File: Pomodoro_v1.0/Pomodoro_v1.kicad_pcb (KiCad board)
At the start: 2 copper layers, 70 x 50 mm, 91 parts, among them J1 BATT, J13 SWIM, J3 USB_OTG, J5 UART, M1 MOUNTING-HOLE, M2 MOUNTING-HOLE, M3 MOUNTING-HOLE, M4 MOUNTING-HOLE, Q1 BC807, Q2 BC807, SW1 SLIDER, SW2 BUTTON_SPST, U1 MCP73833, U2 TPS62260, U3 STM8L151C2T6, U4 AS1122

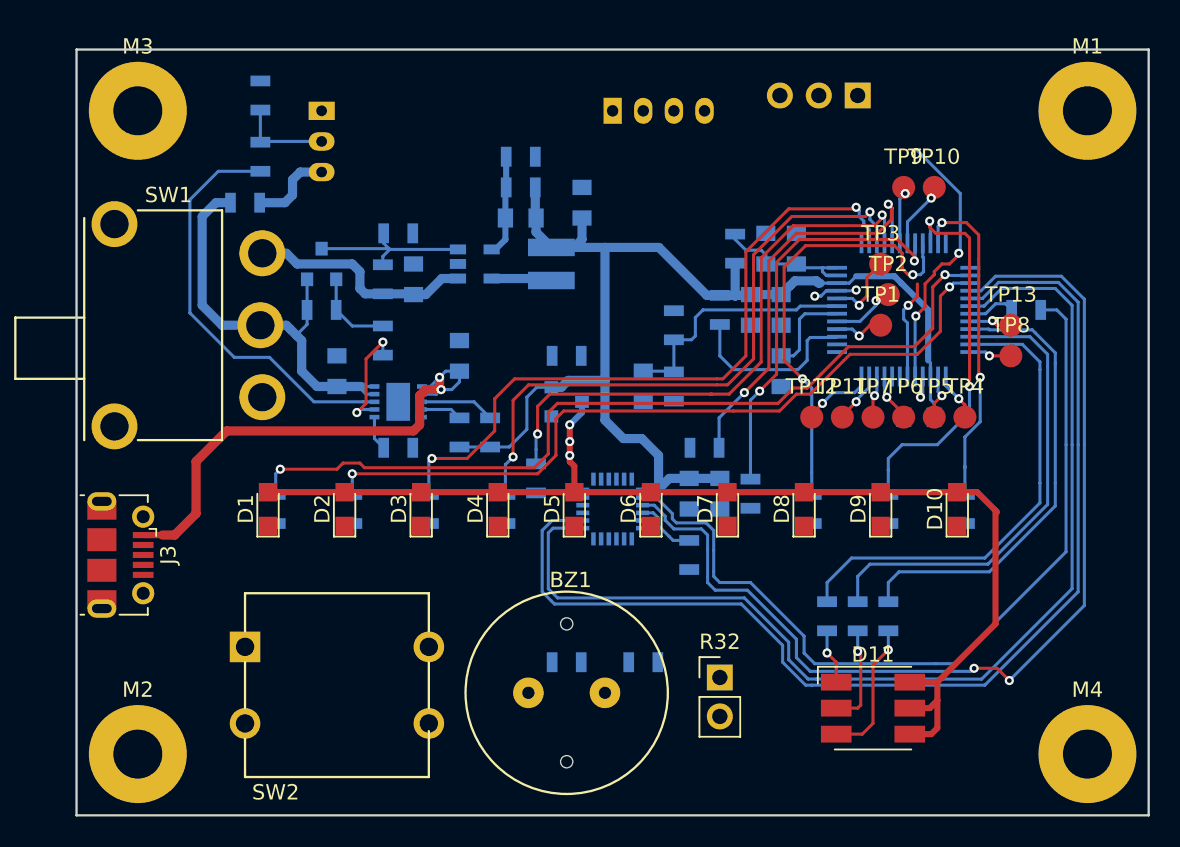
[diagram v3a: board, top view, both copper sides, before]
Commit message: all signals are routed, need to fix a few GND connections
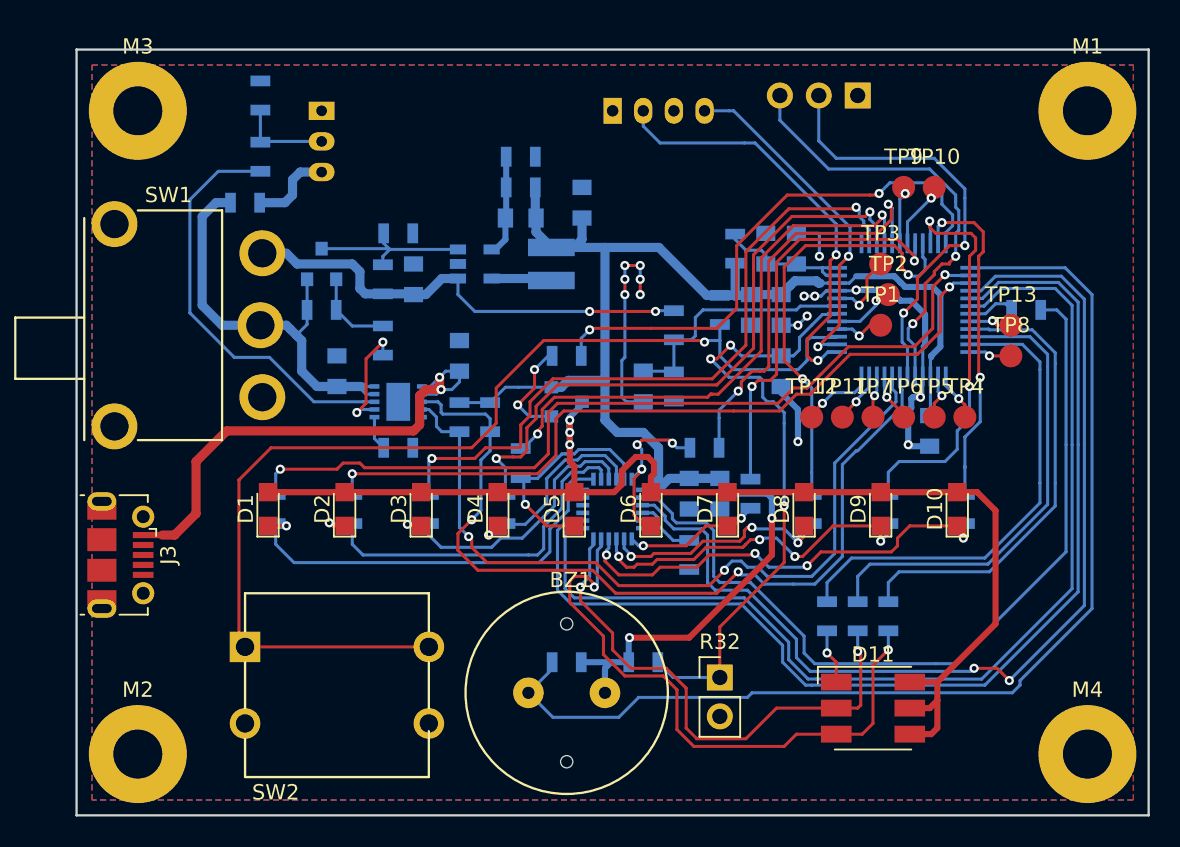
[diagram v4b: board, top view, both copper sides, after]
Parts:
- moved R6 1.41 mm to (57.0, 87.0)
- moved C6 1.14 mm to (83.7, 84.9), turned to 270 degrees
- moved R24 1.00 mm to (55.0, 84.0), turned to 270 degrees
- moved R25 1.00 mm to (53.0, 84.0), turned to 270 degrees
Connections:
- net /D0_0 renamed /DO_0
- U4 pad 10: /D0_3 -> /DO_3
- U4 pad 11: /D0_4 -> /DO_4
- U4 pad 12: /D0_5 -> /DO_5
- U4 pad 15: /AS_RST -> (no net)
- U4 pad 19: /D0_6 -> /DO_6
- U4 pad 20: /D0_7 -> /DO_7
- U4 pad 21: /D0_8 -> /DO_8
- U4 pad 22: /D0_9 -> /DO_9
- U4 pad 23: /D0_10 -> /DO_10
- U4 pad 24: /D0_11 -> /DO_11
- U4 pad 8: /D0_1 -> /DO_1
- U4 pad 9: /D0_2 -> /DO_2
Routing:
- net /BUZZER: track 0.00 -> 72.4 mm
- net /BUTTON: track 11.7 -> 71.4 mm, vias 0 -> 1
- net /STAT1: track 4.88 -> 56.1 mm, vias 0 -> 2
- net /STAT2: track 2.68 -> 51.1 mm, vias 0 -> 2
- net GND: track 4.28 -> 41.5 mm, vias 3 -> 15
- net /PWM_BRIGHTNESS: track 0.00 -> 35.3 mm, vias 0 -> 2
- net /V_LDR: track 5.96 -> 40.9 mm, vias 0 -> 3
- net /DO_10: track 9.15 -> 39.9 mm, vias 1 -> 2
- net /DO_9: track 0.00 -> 29.2 mm, vias 0 -> 4
- net /DO_0: track 0.00 -> 28.7 mm, vias 0 -> 1
- net /SWIM: track 0.00 -> 27.9 mm, vias 0 -> 2
- net /DO_11: track 6.62 -> 34.4 mm, vias 1 -> 2
- net VCC: track 80.4 -> 105.9 mm, vias 0 -> 2
- net /DO_1: track 0.00 -> 25.4 mm, vias 0 -> 1
- net /DO_8: track 0.00 -> 23.2 mm, vias 0 -> 4
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- added copper zone on B.Cu, net GND
- added copper zone on F.Cu, net GND

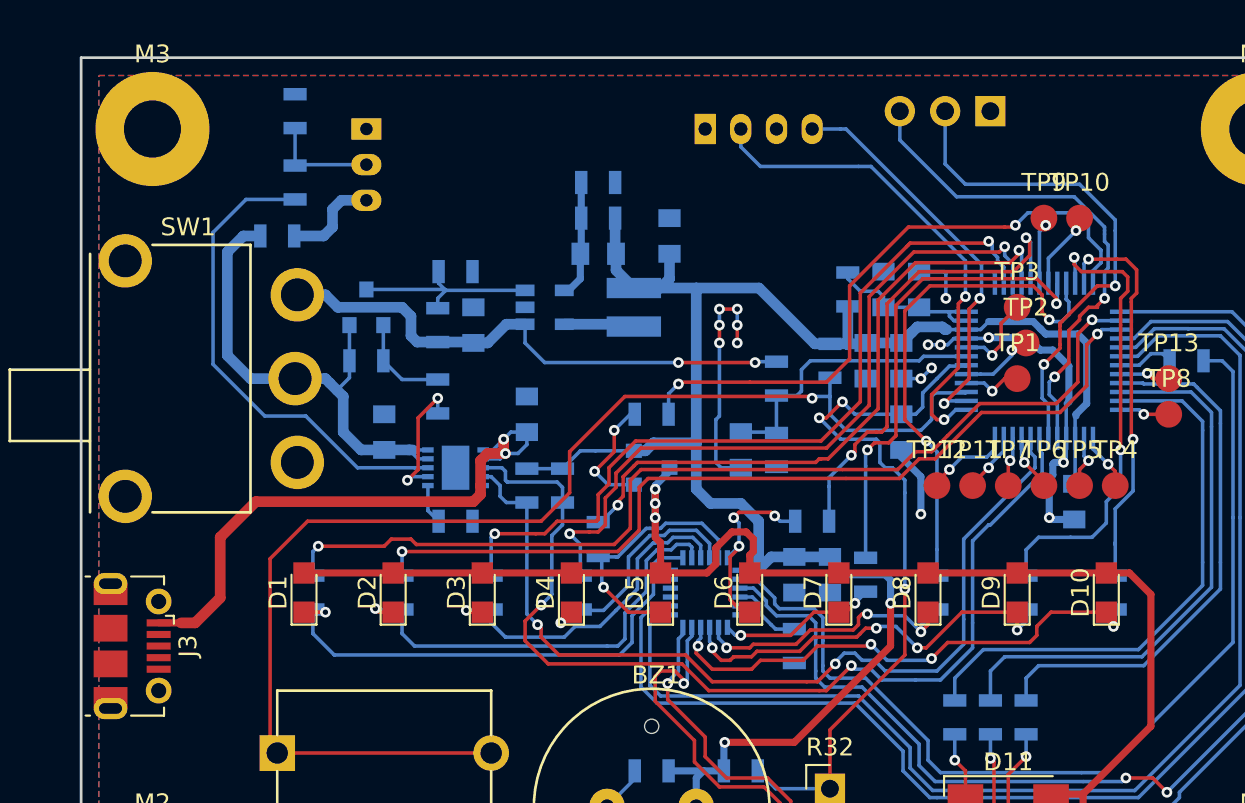
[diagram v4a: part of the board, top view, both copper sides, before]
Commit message: finish GND fixes, board is ready for manufacturing
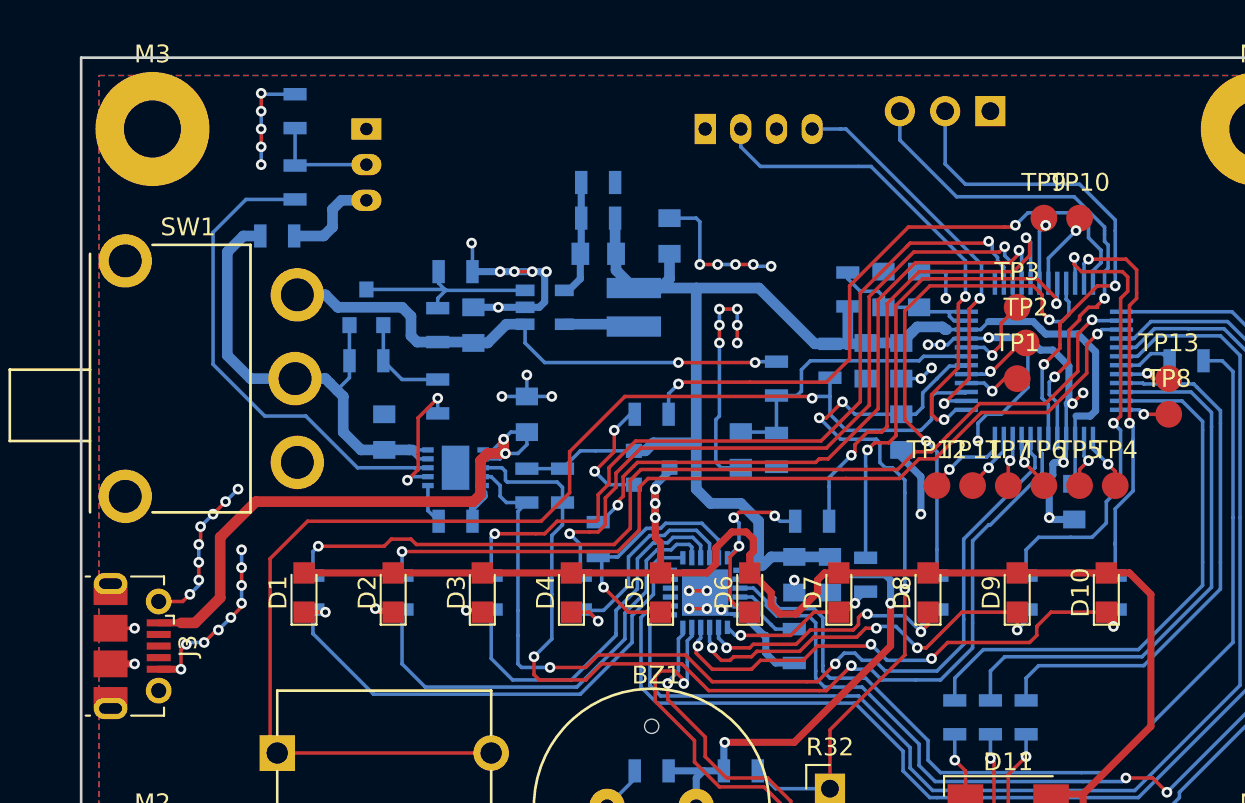
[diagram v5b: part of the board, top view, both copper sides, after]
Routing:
- net GND: track 41.5 -> 121.5 mm, vias 15 -> 62
- net /DO_2: track 19.4 -> 23.4 mm
- net /DO_1: track 25.4 -> 28.3 mm
- net Net-(D1-Pad2): track 82.1 -> 84.9 mm
- net /STAT2: track 51.1 -> 53.4 mm
- net /DO_0: track 28.7 -> 30.5 mm
- net /STAT1: track 56.1 -> 57.2 mm
- net /DO_3: track 13.4 -> 14.5 mm
- net VCC: track 105.9 -> 106.8 mm

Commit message: Add via stitching + silkscreen placement
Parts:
- added REF**: VIA-0.6mm-0.3mm, VIA:VIA-0.6mm-0.3mm, F.Cu at (82.0, 62.0)
- added REF**: VIA-0.6mm-0.3mm, VIA:VIA-0.6mm-0.3mm, F.Cu at (63.0, 62.0)
- added REF**: VIA-0.6mm-0.3mm, VIA:VIA-0.6mm-0.3mm, F.Cu at (61.0, 62.0)
- added REF**: VIA-0.6mm-0.3mm, VIA:VIA-0.6mm-0.3mm, F.Cu at (59.0, 62.0)
- added REF**: VIA-0.6mm-0.3mm, VIA:VIA-0.6mm-0.3mm, F.Cu at (57.0, 62.0)
- added REF**: VIA-0.6mm-0.3mm, VIA:VIA-0.6mm-0.3mm, F.Cu at (55.0, 62.0)
- added REF**: VIA-0.6mm-0.3mm, VIA:VIA-0.6mm-0.3mm, F.Cu at (53.0, 62.0)
- added REF**: VIA-0.6mm-0.3mm, VIA:VIA-0.6mm-0.3mm, F.Cu at (51.0, 62.0)
- added REF**: VIA-0.6mm-0.3mm, VIA:VIA-0.6mm-0.3mm, F.Cu at (49.0, 62.0)
- added REF**: VIA-0.6mm-0.3mm, VIA:VIA-0.6mm-0.3mm, F.Cu at (47.0, 62.0)
- added REF**: VIA-0.6mm-0.3mm, VIA:VIA-0.6mm-0.3mm, F.Cu at (45.0, 62.0)
- added REF**: VIA-0.6mm-0.3mm, VIA:VIA-0.6mm-0.3mm, F.Cu at (84.0, 62.0)
- added REF**: VIA-0.6mm-0.3mm, VIA:VIA-0.6mm-0.3mm, F.Cu at (43.0, 62.0)
- added REF**: VIA-0.6mm-0.3mm, VIA:VIA-0.6mm-0.3mm, F.Cu at (36.0, 62.0)
- added REF**: VIA-0.6mm-0.3mm, VIA:VIA-0.6mm-0.3mm, F.Cu at (30.0, 99.0)
- added REF**: VIA-0.6mm-0.3mm, VIA:VIA-0.6mm-0.3mm, F.Cu at (30.0, 82.0)
- added REF**: VIA-0.6mm-0.3mm, VIA:VIA-0.6mm-0.3mm, F.Cu at (30.0, 80.0)
- added REF**: VIA-0.6mm-0.3mm, VIA:VIA-0.6mm-0.3mm, F.Cu at (30.0, 78.0)
- added REF**: VIA-0.6mm-0.3mm, VIA:VIA-0.6mm-0.3mm, F.Cu at (30.0, 76.0)
- added REF**: VIA-0.6mm-0.3mm, VIA:VIA-0.6mm-0.3mm, F.Cu at (30.0, 74.0)
- added REF**: VIA-0.6mm-0.3mm, VIA:VIA-0.6mm-0.3mm, F.Cu at (96.0, 102.0)
- added REF**: VIA-0.6mm-0.3mm, VIA:VIA-0.6mm-0.3mm, F.Cu at (96.0, 100.0)
- added REF**: VIA-0.6mm-0.3mm, VIA:VIA-0.6mm-0.3mm, F.Cu at (86.0, 62.0)
- added REF**: VIA-0.6mm-0.3mm, VIA:VIA-0.6mm-0.3mm, F.Cu at (96.0, 98.0)
- added REF**: VIA-0.6mm-0.3mm, VIA:VIA-0.6mm-0.3mm, F.Cu at (96.0, 96.0)
- added REF**: VIA-0.6mm-0.3mm, VIA:VIA-0.6mm-0.3mm, F.Cu at (96.0, 94.0)
- added REF**: VIA-0.6mm-0.3mm, VIA:VIA-0.6mm-0.3mm, F.Cu at (96.0, 92.0)
- added REF**: VIA-0.6mm-0.3mm, VIA:VIA-0.6mm-0.3mm, F.Cu at (96.0, 90.0)
- added REF**: VIA-0.6mm-0.3mm, VIA:VIA-0.6mm-0.3mm, F.Cu at (96.0, 88.0)
- added REF**: VIA-0.6mm-0.3mm, VIA:VIA-0.6mm-0.3mm, F.Cu at (96.0, 86.0)
- added REF**: VIA-0.6mm-0.3mm, VIA:VIA-0.6mm-0.3mm, F.Cu at (96.0, 84.0)
- added REF**: VIA-0.6mm-0.3mm, VIA:VIA-0.6mm-0.3mm, F.Cu at (96.0, 82.0)
- added REF**: VIA-0.6mm-0.3mm, VIA:VIA-0.6mm-0.3mm, F.Cu at (96.0, 80.0)
- added REF**: VIA-0.6mm-0.3mm, VIA:VIA-0.6mm-0.3mm, F.Cu at (88.0, 62.0)
- added REF**: VIA-0.6mm-0.3mm, VIA:VIA-0.6mm-0.3mm, F.Cu at (96.0, 78.0)
- added REF**: VIA-0.6mm-0.3mm, VIA:VIA-0.6mm-0.3mm, F.Cu at (96.0, 76.0)
- added REF**: VIA-0.6mm-0.3mm, VIA:VIA-0.6mm-0.3mm, F.Cu at (96.0, 74.0)
- added REF**: VIA-0.6mm-0.3mm, VIA:VIA-0.6mm-0.3mm, F.Cu at (96.0, 72.0)
- added REF**: VIA-0.6mm-0.3mm, VIA:VIA-0.6mm-0.3mm, F.Cu at (96.0, 70.0)
- added REF**: VIA-0.6mm-0.3mm, VIA:VIA-0.6mm-0.3mm, F.Cu at (96.0, 68.0)
- added REF**: VIA-0.6mm-0.3mm, VIA:VIA-0.6mm-0.3mm, F.Cu at (90.0, 108.0)
- added REF**: VIA-0.6mm-0.3mm, VIA:VIA-0.6mm-0.3mm, F.Cu at (88.0, 108.0)
- added REF**: VIA-0.6mm-0.3mm, VIA:VIA-0.6mm-0.3mm, F.Cu at (86.0, 108.0)
- added REF**: VIA-0.6mm-0.3mm, VIA:VIA-0.6mm-0.3mm, F.Cu at (84.0, 108.0)
- added REF**: VIA-0.6mm-0.3mm, VIA:VIA-0.6mm-0.3mm, F.Cu at (90.0, 62.0)
- added REF**: VIA-0.6mm-0.3mm, VIA:VIA-0.6mm-0.3mm, F.Cu at (82.0, 108.0)
- added REF**: VIA-0.6mm-0.3mm, VIA:VIA-0.6mm-0.3mm, F.Cu at (80.0, 108.0)
- added REF**: VIA-0.6mm-0.3mm, VIA:VIA-0.6mm-0.3mm, F.Cu at (78.0, 108.0)
- added REF**: VIA-0.6mm-0.3mm, VIA:VIA-0.6mm-0.3mm, F.Cu at (76.0, 108.0)
- added REF**: VIA-0.6mm-0.3mm, VIA:VIA-0.6mm-0.3mm, F.Cu at (74.0, 108.0)
- added REF**: VIA-0.6mm-0.3mm, VIA:VIA-0.6mm-0.3mm, F.Cu at (72.0, 108.0)
- added REF**: VIA-0.6mm-0.3mm, VIA:VIA-0.6mm-0.3mm, F.Cu at (70.0, 108.0)
- added REF**: VIA-0.6mm-0.3mm, VIA:VIA-0.6mm-0.3mm, F.Cu at (68.0, 108.0)
- added REF**: VIA-0.6mm-0.3mm, VIA:VIA-0.6mm-0.3mm, F.Cu at (66.0, 108.0)
- added REF**: VIA-0.6mm-0.3mm, VIA:VIA-0.6mm-0.3mm, F.Cu at (64.0, 108.0)
- added REF**: VIA-0.6mm-0.3mm, VIA:VIA-0.6mm-0.3mm, F.Cu at (71.0, 62.0)
- added REF**: VIA-0.6mm-0.3mm, VIA:VIA-0.6mm-0.3mm, F.Cu at (62.0, 108.0)
- added REF**: VIA-0.6mm-0.3mm, VIA:VIA-0.6mm-0.3mm, F.Cu at (60.0, 108.0)
- added REF**: VIA-0.6mm-0.3mm, VIA:VIA-0.6mm-0.3mm, F.Cu at (58.0, 108.0)
- added REF**: VIA-0.6mm-0.3mm, VIA:VIA-0.6mm-0.3mm, F.Cu at (56.0, 108.0)
- added REF**: VIA-0.6mm-0.3mm, VIA:VIA-0.6mm-0.3mm, F.Cu at (54.0, 108.0)
- added REF**: VIA-0.6mm-0.3mm, VIA:VIA-0.6mm-0.3mm, F.Cu at (52.0, 108.0)
- added REF**: VIA-0.6mm-0.3mm, VIA:VIA-0.6mm-0.3mm, F.Cu at (50.0, 108.0)
- added REF**: VIA-0.6mm-0.3mm, VIA:VIA-0.6mm-0.3mm, F.Cu at (48.0, 108.0)
- added REF**: VIA-0.6mm-0.3mm, VIA:VIA-0.6mm-0.3mm, F.Cu at (46.0, 108.0)
- added REF**: VIA-0.6mm-0.3mm, VIA:VIA-0.6mm-0.3mm, F.Cu at (44.0, 108.0)
- added REF**: VIA-0.6mm-0.3mm, VIA:VIA-0.6mm-0.3mm, F.Cu at (69.0, 62.0)
- added REF**: VIA-0.6mm-0.3mm, VIA:VIA-0.6mm-0.3mm, F.Cu at (42.0, 108.0)
- added REF**: VIA-0.6mm-0.3mm, VIA:VIA-0.6mm-0.3mm, F.Cu at (40.0, 108.0)
- added REF**: VIA-0.6mm-0.3mm, VIA:VIA-0.6mm-0.3mm, F.Cu at (38.0, 108.0)
- added REF**: VIA-0.6mm-0.3mm, VIA:VIA-0.6mm-0.3mm, F.Cu at (36.0, 108.0)
- added REF**: VIA-0.6mm-0.3mm, VIA:VIA-0.6mm-0.3mm, F.Cu at (67.0, 62.0)
- added REF**: VIA-0.6mm-0.3mm, VIA:VIA-0.6mm-0.3mm, F.Cu at (65.0, 62.0)
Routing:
- net GND: track 121.5 -> 119.4 mm, vias 62 -> 59
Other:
- board text added: "+"
- board text added: "-"
- board text added: "GND"
- board text added: "M_RX"
- board text added: "M_TX"
- board text added: "NRST"
- board text added: "Productivity Timer v1.0 08.2018 | L. Meyer www.lukemeyer.me"
- board text added: "SWIM"
- board text added: "T"
